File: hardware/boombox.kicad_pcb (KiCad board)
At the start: 4 copper layers, 125 x 107.9 mm, 92 parts, among them J1 Micro_SD_Card_Det1, J2 AudioJack4, J3 Battery, J4 USB_C_Receptacle_USB2.0_16P, U1 Pico, U10 MAX98365A, U2 TMAG5231, U3 TMAG5231, U4 TMAG5231, U5 TMAG5231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

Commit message: Almost done TM
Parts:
- removed C5, C6, C7, C8, C9: 1nF, Capacitor_SMD:C_0402_1005Metric_Pad0.74x0.62mm_HandSolder
- removed D6, D7, D8: D_Dual_CommonCathode_AAK_Split, Package_TO_SOT_SMD:SOT-23
- removed J3: Battery, boombox:EBAA02C
- removed LS1: Speaker, boombox:EBAA02C
- removed the REF** at (166.0, 36.4)
- removed the REF** at (144.0, 36.4)
- removed the REF** at (199.7, 71.7)
- removed RV1: 500k, boombox:Degson 3 Pin
- removed TP10, TP9: ~, boombox:TestPoint_Pad_2.0x2.0mm
- removed TP11: TestPoint_Small, boombox:TestPoint_Pad_2.0x2.0mm
- added J5: Screw_Terminal_01x07, boombox:1990054, B.Cu at (196.1, 76.7)
- J2: value AudioJack4 -> Screw_Terminal_01x07; footprint boombox:EBAA02C_Audio -> boombox:1990054
- TP1, TP2, TP3, TP4, TP5, TP6, TP7, TP8: value ~ -> TestPoint_Small; moved to B.Cu
- TP12: moved to B.Cu
- moved TP12 90.5 mm to (167.0, 44.3)
- moved C11 53.8 mm to (133.2, 71.7), turned to 180 degrees
- moved J2 52.5 mm to (183.3, 125.0)
- moved TP7 46.6 mm to (183.5, 104.8)
- moved D11 43.7 mm to (196.7, 87.2)
- moved TP6 39.9 mm to (183.7, 100.3), turned to 180 degrees
- moved C17 34.7 mm to (110.8, 91.2)
- moved TP8 31.3 mm to (143.0, 44.3), turned to 180 degrees
- moved TP4 26.6 mm to (159.0, 44.3), turned to 180 degrees
- moved TP2 26.2 mm to (151.0, 44.3), turned to 180 degrees
- moved C21 24.2 mm to (197.1, 107.4), turned to -90 degrees
- moved C20 21.7 mm to (171.6, 117.2)
- moved TP3 21.3 mm to (155.0, 44.3), turned to 180 degrees
- moved TP1 19.6 mm to (147.0, 44.3), turned to 180 degrees
- moved TP5 19.2 mm to (163.0, 44.3), turned to 180 degrees
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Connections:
- Q2 pad 3: /Power/BUTTONS0 -> /Power/BTN_LATCH
- Q5 pad 1: /Power/BUTTONS0 -> /Power/BTN_LATCH
- R3 pad 1: /Power/BUTTONS0 -> /Power/BTN_LATCH
- S1 pad 3: (no net) -> unconnected-(S1-NO_1-Pad3)
- S1 pad 6: (no net) -> unconnected-(S1-NO_2-Pad6)
- S2 pad 1: Net-(S2-NC_1) -> Net-(S1-NC_1)
- S2 pad 3: (no net) -> unconnected-(S2-NO_1-Pad3)
- S2 pad 6: (no net) -> unconnected-(S2-NO_2-Pad6)
- S3 pad 1: Net-(S3-NC_1) -> Net-(S1-NC_1)
- S3 pad 3: (no net) -> unconnected-(S3-NO_1-Pad3)
- S3 pad 6: (no net) -> unconnected-(S3-NO_2-Pad6)
- S4 pad 1: Net-(S4-NC_1) -> Net-(S1-NC_1)
- S4 pad 3: (no net) -> unconnected-(S4-NO_1-Pad3)
- S4 pad 6: (no net) -> unconnected-(S4-NO_2-Pad6)
- S5 pad 1: Net-(S5-NC_1) -> Net-(S1-NC_1)
- S5 pad 3: (no net) -> unconnected-(S5-NO_1-Pad3)
- S5 pad 6: (no net) -> unconnected-(S5-NO_2-Pad6)
- TP1 pad 1: Net-(S1-NC_1) -> Net-(S1-NC_2)
- TP2 pad 1: /Power/BUTTONS0 -> Net-(S2-NC_2)
- TP3 pad 1: Net-(S2-NC_1) -> Net-(S3-NC_2)
- TP4 pad 1: /Power/BUTTONS0 -> Net-(S4-NC_2)
- TP5 pad 1: Net-(S3-NC_1) -> Net-(S5-NC_2)
- TP6 pad 1: /Power/BUTTONS0 -> Net-(D12-A)
- TP7 pad 1: Net-(S4-NC_1) -> GND
- TP8 pad 1: /Power/BUTTONS0 -> Net-(S1-NC_1)
- U1 pad 15: Net-(S1-NC_2) -> Net-(J2-Pin_7)
- U1 pad 16: Net-(S2-NC_2) -> Net-(J2-Pin_6)
- U1 pad 17: Net-(S3-NC_2) -> Net-(J2-Pin_5)
- U1 pad 19: Net-(S4-NC_2) -> Net-(J2-Pin_4)
- U1 pad 20: Net-(S5-NC_2) -> Net-(J2-Pin_3)
- U8 pad A2: Net-(U8-OUTN) -> Net-(J5-Pin_4)
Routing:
- net /Power/BTN_LATCH: track 0.00 -> 114.3 mm, vias 0 -> 1
- net BTN_PWR: track 0.00 -> 109.3 mm, vias 0 -> 1
- net Net-(S1-NC_1): track 0.00 -> 101.9 mm, vias 0 -> 1
- net Net-(J2-Pin_6): track 0.00 -> 77.8 mm, vias 0 -> 1
- net Net-(J2-Pin_4): track 0.00 -> 77.8 mm, vias 0 -> 1
- net Net-(J2-Pin_3): track 0.00 -> 75.2 mm, vias 0 -> 1
- net Net-(J2-Pin_5): track 0.00 -> 73.3 mm, vias 0 -> 1
- net Net-(J2-Pin_7): track 0.00 -> 61.8 mm, vias 0 -> 1
- net /Power/MAG_SENSOR4: track 105.8 -> 55.8 mm
- net /Power/MAG_SENSOR3: track 119.6 -> 72.8 mm
- net Net-(S1-NC_2): track 0.00 -> 41.0 mm
- net Net-(S5-NC_2): track 0.00 -> 35.5 mm
- net /Power/CLOCK_ALARM: track 60.5 -> 95.6 mm
- net /Power/POWER IN: track 65.3 -> 41.1 mm, vias 3 -> 4
- net Net-(S2-NC_2): track 0.00 -> 23.0 mm
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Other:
- outline, holes or cut-outs redrawn
- board text added: "Batt+"
- board text added: "Batt-"

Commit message: Fixing warnings
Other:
- board text added: "1. SPK+ 2. SPK- 3. AUX+ 4. AUX- 5. POT+ 6. POT→ 7. POT-"
- board text added: "1. SW_PWR 2. WAKE 3. SW5 4. SW4 5. SW3 6. SW2 7. SW1"
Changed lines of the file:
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@@
 		(tags "capacitor handsolder")
 		(property "Reference" "C11"
-			(at -0.625 1.175 360)
+			(at -0.625 1.175 0)
 			(layer "F.SilkS")
 			(effects
@@
 		)
 		(property "Value" "0.1uF"
-			(at 0 1.16 360)
+			(at 0 1.16 0)
 			(layer "F.Fab")
 			(hide yes)
@@
 		)
 		(fp_text user "${REFERENCE}"
-			(at 0 0 360)
+			(at 0 0 0)
 			(layer "F.Fab")
 			(effects
@@
 		(tags "capacitor handsolder")
 		(property "Reference" "C10"
-			(at 0 -1.16 360)
+			(at 0 -1.16 0)
 			(layer "F.SilkS")
 			(effects
@@
 		)
 		(property "Value" "0.1uF"
-			(at 0 1.16 360)
+			(at 0 1.16 0)
 			(layer "F.Fab")
 			(hide yes)
@@
 		)
 		(fp_text user "${REFERENCE}"
-			(at 0 0 360)
+			(at 0 0 0)
 			(layer "F.Fab")
 			(effects
@@
 		(tags "SOD-123")
 		(property "Reference" "D11"
-			(at 0.425 2.325 360)
+			(at 0.425 2.325 0)
 			(layer "F.SilkS")
 			(hide yes)
@@
 		)
 		(property "Value" "D_Schottky"
-			(at 0 2.1 360)
+			(at 0 2.1 0)
 			(layer "F.Fab")
 			(hide yes)
@@
 		)
 		(fp_text user "${REFERENCE}"
-			(at 0 -1.85 360)
+			(at 0 -1.85 0)
 			(layer "F.SilkS")
 			(effects
@@
 			(at -0.020005 -2.282797 90)
 			(layer "F.SilkS")
+			(hide yes)
 			(effects
 				(font
@@
 		(tags "Connector")
 		(property "Reference" "J5"
-			(at 6.375 1.3 0)
+			(at 7.2 1.3 0)
 			(layer "B.SilkS")
 			(effects
@@
 			(layer "B.Fab")
 		)
-		(fp_text user "${REFERENCE}"
-			(at 6.375 1.3 0)
-			(layer "B.Fab")
-			(effects
-				(font
-					(size 1.27 1.27)
-					(thickness 0.254)
-				)
-				(justify mirror)
-			)
-		)
 		(pad "1" thru_hole circle
 			(at 0 0 180)
@@
 		(tags "SOT TO_SOT_SMD")
 		(property "Reference" "U3"
-			(at 0 -2.6 0)
+			(at 2.975 1.45 0)
 			(layer "B.SilkS")
 			(effects
@@
 		)
 	)
+	(gr_text "1. SW_PWR\n2. WAKE\n3. SW5\n4. SW4\n5. SW3\n6. SW2\n7. SW1\n"
+		(at 177.075 131.925 0)
+		(layer "B.SilkS")
+		(effects
+			(font
+				(size 1 1)
+				(thickness 0.1)
+			)
+			(justify left bottom mirror)
+		)
+	)
+	(gr_text "1. SPK+\n2. SPK-\n3. AUX+\n4. AUX-\n5. POT+\n6. POT→\n7. POT-\n"
+		(at 177.45 79.775 0)
+		(layer "B.SilkS")
+		(effects
+			(font
+				(size 1 1)
+				(thickness 0.1)
+			)
+			(justify left bottom mirror)
+		)
+	)
 	(gr_text "Boomy Jr. V1.0"
 		(at 104.1 126.05 0)
@@
 	)
 	(segment
-		(start 181.93375 83.445748)
-		(end 181.83375 83.545748)
-		(width 0.15)
+		(start 182.117422 84.317422)
+		(end 182.323892 84.317422)
+		(width 0.2)
 		(layer "F.Cu")
 		(net 8)
@@
 	)
 	(segment
+		(start 181.93375 82.60875)
+		(end 181.83375 82.70875)
+		(width 0.2)
+		(layer "F.Cu")
+		(net 8)
+	)
+	(segment
 		(start 176.98375 82.5175)
 		(end 176.98375 83.445748)
@@
 	)
 	(segment
-		(start 181.83375 83.9675)
-		(end 182.183753 84.317503)
+		(start 176.88375 83.545748)
+		(end 176.88375 83.9675)
 		(width 0.15)
 		(layer "F.Cu")
@@
 	)
 	(segment
-		(start 176.88375 83.545748)
-		(end 176.88375 83.9675)
-		(width 0.15)
+		(start 182.323892 84.317422)
+		(end 182.440935 84.317422)
+		(width 0.2)
 		(layer "F.Cu")
 		(net 8)
@@
 	)
 	(segment
-		(start 181.93375 82.5175)
-		(end 181.93375 83.445748)
-		(width 0.15)
-		(layer "F.Cu")
-		(net 8)
-	)
-	(segment
 		(start 175.14625 83.9625)
 		(end 175.15125 83.9675)
@@
 	)
 	(segment
-		(start 182.80875 83.9425)
-		(end 182.433747 84.317503)
-		(width 0.15)
+		(start 181.83375 82.70875)
+		(end 181.83375 84.03375)
+		(width 0.2)
 		(layer "F.Cu")
 		(net 8)
@@
 	)
 	(segment
+		(start 181.83375 84.03375)
+		(end 182.117422 84.317422)
+		(width 0.2)
+		(layer "F.Cu")
+		(net 8)
+	)
+	(segment
 		(start 137.9919 80.3075)
 		(end 137.9919 78.82)
@@
 	)
 	(segment
-		(start 182.183753 84.317503)
-		(end 182.33375 84.317503)
-		(width 0.15)
-		(layer "F.Cu")
-		(net 8)
-	)
-	(segment
 		(start 177.85875 83.9425)
 		(end 177.483747 84.317503)
@@
 	)
 	(segment
-		(start 181.83375 83.545748)
-		(end 181.83375 83.9675)
-		(width 0.15)
-		(layer "F.Cu")
-		(net 8)
-	)
-	(segment
 		(start 160.2625 80.5625)
 		(end 160.2 80.5)
@@
 	)
 	(segment
-		(start 182.433747 84.317503)
-		(end 182.33375 84.317503)
-		(width 0.15)
+		(start 182.440935 84.317422)
+		(end 182.812304 83.946053)
+		(width 0.2)
+		(layer "F.Cu")
+		(net 8)
+	)
+	(segment
+		(start 181.93375 82.5175)
+		(end 181.93375 82.60875)
+		(width 0.2)
 		(layer "F.Cu")
 		(net 8)
@@
 	)
 	(via
-		(at 182.33375 84.317503)
-		(size 0.4)
-		(drill 0.3)
-		(layers "F.Cu" "B.Cu")
-		(net 8)
-	)
-	(via
 		(at 181.225 86.925)
 		(size 0.6)
@@
 		(layers "F.Cu" "B.Cu")
 		(net 8)
+	)
+	(via
+		(at 182.323892 84.317422)
+		(size 0.4)
+		(drill 0.3)
+		(layers "F.Cu" "B.Cu")
+		(net 8)

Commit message: Fixed warnings
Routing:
- net Net-(U10-DAI1): vias 5 -> 4
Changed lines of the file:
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@@
 	)
 	(gr_text "1. SW_PWR\n2. WAKE\n3. SW5\n4. SW4\n5. SW3\n6. SW2\n7. SW1\n"
-		(at 177.075 131.925 0)
+		(at 179.825 131.525 0)
 		(layer "B.SilkS")
 		(effects
@@
 	)
 	(gr_text "1. SPK+\n2. SPK-\n3. AUX+\n4. AUX-\n5. POT+\n6. POT→\n7. POT-\n"
-		(at 177.45 79.775 0)
+		(at 179.425 79.75 0)
 		(layer "B.SilkS")
 		(effects
@@
 	)
 	(segment
+		(start 182.308357 84.45)
+		(end 182.812304 83.946053)
+		(width 0.2)
+		(layer "F.Cu")
+		(net 8)
+	)
+	(segment
 		(start 175.14625 81.20375)
 		(end 175.15 81.2)
@@
 	)
 	(segment
-		(start 182.117422 84.317422)
-		(end 182.323892 84.317422)
-		(width 0.2)
-		(layer "F.Cu")
-		(net 8)
-	)
-	(segment
 		(start 176.88375 83.9675)
 		(end 177.233753 84.317503)
@@
 	)
 	(segment
+		(start 181.975 84.45)
+		(end 182.308357 84.45)
+		(width 0.2)
+		(layer "F.Cu")
+		(net 8)
+	)
+	(segment
 		(start 177.78375 83.445748)
 		(end 177.85875 83.520748)
@@
 	)
 	(segment
+		(start 181.83375 84.03375)
+		(end 181.975 84.175)
+		(width 0.2)
+		(layer "F.Cu")
+		(net 8)
+	)
+	(segment
 		(start 176.98375 82.5175)
 		(end 176.98375 83.445748)
@@
 	)
 	(segment
-		(start 176.88375 83.545748)
-		(end 176.88375 83.9675)
-		(width 0.15)
+		(start 181.975 84.175)
+		(end 181.975 84.45)
+		(width 0.2)
 		(layer "F.Cu")
 		(net 8)
 	)
 	(segment
-		(start 182.323892 84.317422)
-		(end 182.440935 84.317422)
-		(width 0.2)
+		(start 176.88375 83.545748)
+		(end 176.88375 83.9675)
+		(width 0.15)
 		(layer "F.Cu")
 		(net 8)
@@
 	)
 	(segment
-		(start 181.83375 84.03375)
-		(end 182.117422 84.317422)
-		(width 0.2)
-		(layer "F.Cu")
-		(net 8)
-	)
-	(segment
 		(start 137.9919 80.3075)
 		(end 137.9919 78.82)
@@
 	)
 	(segment
-		(start 182.440935 84.317422)
-		(end 182.812304 83.946053)
-		(width 0.2)
-		(layer "F.Cu")
-		(net 8)
-	)
-	(segment
 		(start 181.93375 82.5175)
 		(end 181.93375 82.60875)
@@
 	)
 	(via
-		(at 137.8994 80.4)
-		(size 1)
-		(drill 0.6)
+		(at 181.975 84.45)
+		(size 0.4)
+		(drill 0.3)
 		(layers "F.Cu" "B.Cu")
 		(net 8)
 	)
 	(via
-		(at 182.323892 84.317422)
-		(size 0.4)
-		(drill 0.3)
+		(at 137.8994 80.4)
+		(size 1)
+		(drill 0.6)
 		(layers "F.Cu" "B.Cu")
 		(net 8)
@@
 	)
 	(via
-		(at 180.28375 86.2175)
-		(size 0.4)
-		(drill 0.3)
-		(layers "F.Cu" "B.Cu")
-		(net 38)
-	)
-	(via
 		(at 184.23375 82.1175)
 		(size 0.4)
@@
 	)
 	(segment
-		(start 180.28375 86.2175)
-		(end 179.88 86.62125)
+		(start 179.88 102.32)
+		(end 177.65 104.55)
 		(width 0.4)
 		(layer "B.Cu")
@@
 	)
 	(segment
-		(start 183.38375 82.9675)
-		(end 180.28375 82.9675)
-		(width 0.1)
+		(start 180.272687 82.972687)
+		(end 180.272687 85.588937)
+		(width 0.4)
 		(layer "B.Cu")
 		(net 38)
 	)
 	(segment
-		(start 179.88 86.62125)
-		(end 179.88 102.32)
+		(start 180.272687 85.588937)
+		(end 180.28375 85.6)
 		(width 0.4)
 		(layer "B.Cu")
@@
 	)
 	(segment
-		(start 184.23375 82.1175)
-		(end 183.38375 82.9675)
-		(width 0.1)
+		(start 180.28375 85.6)
+		(end 179.88 86.00375)
+		(width 0.4)
 		(layer "B.Cu")
 		(net 38)
 	)
 	(segment
-		(start 179.88 102.32)
-		(end 177.65 104.55)
+		(start 179.43375 82.13375)
+		(end 180.272687 82.972687)
 		(width 0.4)
 		(layer "B.Cu")
@@
 	)
 	(segment
-		(start 160.9975 104.5525)
-		(end 161 104.55)
+		(start 179.88 86.00375)
+		(end 179.88 102.32)
 		(width 0.4)
 		(layer "B.Cu")
@@
 	)
 	(segment
-		(start 180.28375 86.2175)
-		(end 180.28375 82.9675)
-		(width 0.1)
+		(start 160.9975 104.5525)
+		(end 161 104.55)
+		(width 0.4)
 		(layer "B.Cu")
 		(net 38)
@@
 	)
 	(segment
-		(start 180.28375 82.9675)
-		(end 179.43375 82.1175)
-		(width 0.1)
+		(start 180.272687 82.972687)
+		(end 183.378563 82.972687)
+		(width 0.4)
+		(layer "B.Cu")
+		(net 38)
+	)
+	(segment
+		(start 183.378563 82.972687)
+		(end 184.23375 82.1175)
+		(width 0.4)
+		(layer "B.Cu")
+		(net 38)
+	)
+	(segment
+		(start 179.43375 82.1175)
+		(end 179.43375 82.13375)
+		(width 0.4)
 		(layer "B.Cu")
 		(net 38)

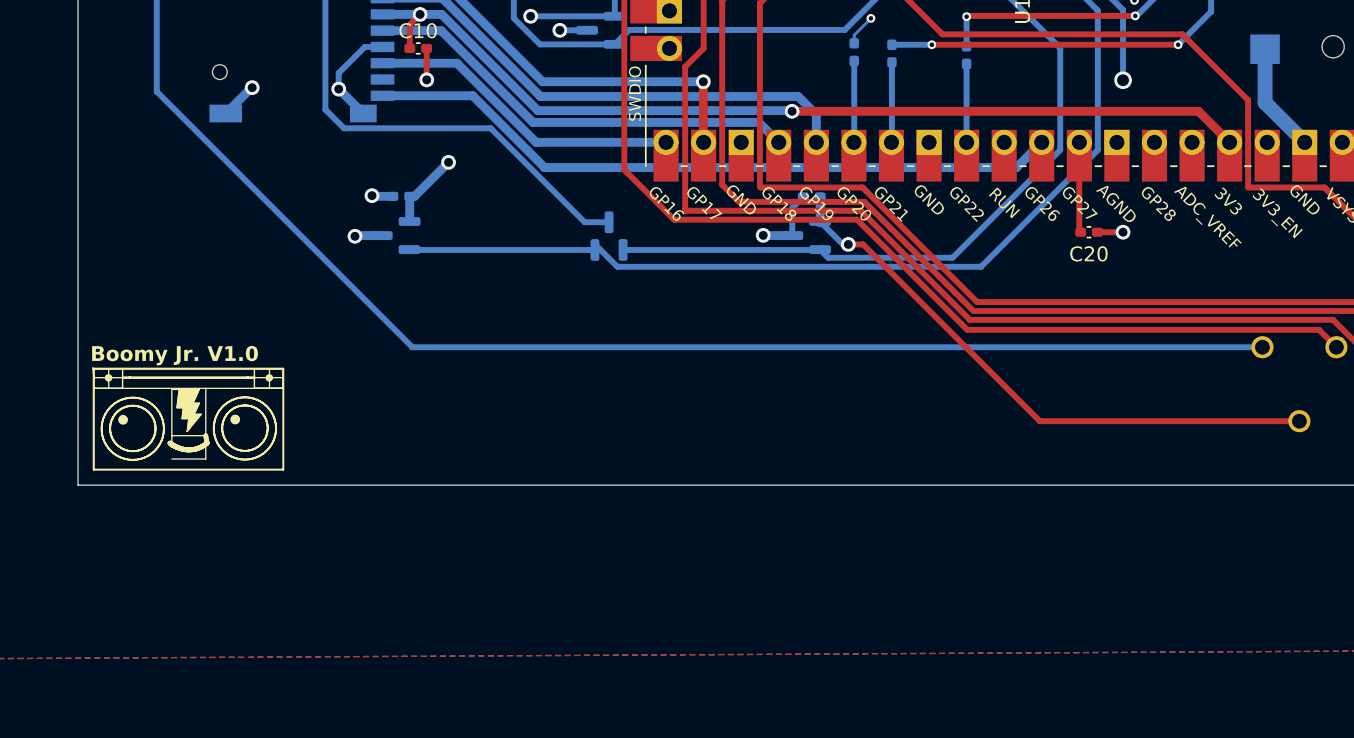
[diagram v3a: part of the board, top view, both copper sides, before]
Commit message: Added debouncing caps
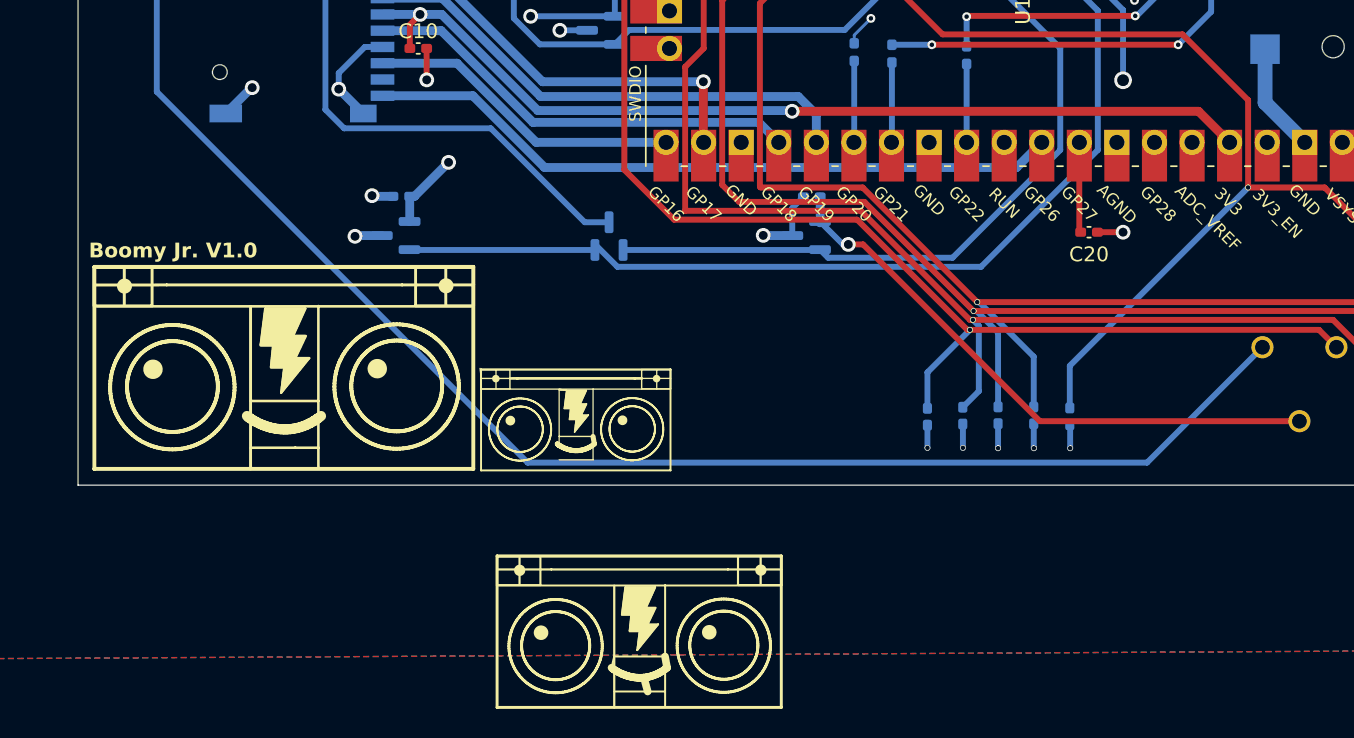
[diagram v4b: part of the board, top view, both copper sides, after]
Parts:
- added C5: .1u, Capacitor_SMD:C_0402_1005Metric_Pad0.74x0.62mm_HandSolder, B.Cu at (160.7, 129.7)
- added C6: .1u, Capacitor_SMD:C_0402_1005Metric_Pad0.74x0.62mm_HandSolder, B.Cu at (163.1, 129.6)
- added C7: .1u, Capacitor_SMD:C_0402_1005Metric_Pad0.74x0.62mm_HandSolder, B.Cu at (165.5, 129.6)
- added C8: .1u, Capacitor_SMD:C_0402_1005Metric_Pad0.74x0.62mm_HandSolder, B.Cu at (167.9, 129.6)
- added C9: .1u, Capacitor_SMD:C_0402_1005Metric_Pad0.74x0.62mm_HandSolder, B.Cu at (170.3, 129.7)
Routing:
- net Net-(J2-Pin_7): track 61.8 -> 81.7 mm, vias 1 -> 2
- net Net-(J2-Pin_6): track 77.8 -> 86.6 mm, vias 1 -> 2
- net GND: track 92.9 -> 100.9 mm, vias 31 -> 36
- net Net-(J2-Pin_5): track 73.3 -> 80.6 mm, vias 1 -> 2
- net Net-(J2-Pin_4): track 77.8 -> 84.3 mm, vias 1 -> 2
- net Net-(J2-Pin_3): track 75.2 -> 81.7 mm, vias 1 -> 2
- net /Power/BTN_LATCH: track 114.3 -> 120.7 mm
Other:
- board text added: "SW1"
- board text added: "SW2"
- board text added: "SW3"
- board text added: "SW4"
- board text added: "SW5"
- board text added: "SW_PWR"
- board text added: "WAKE"

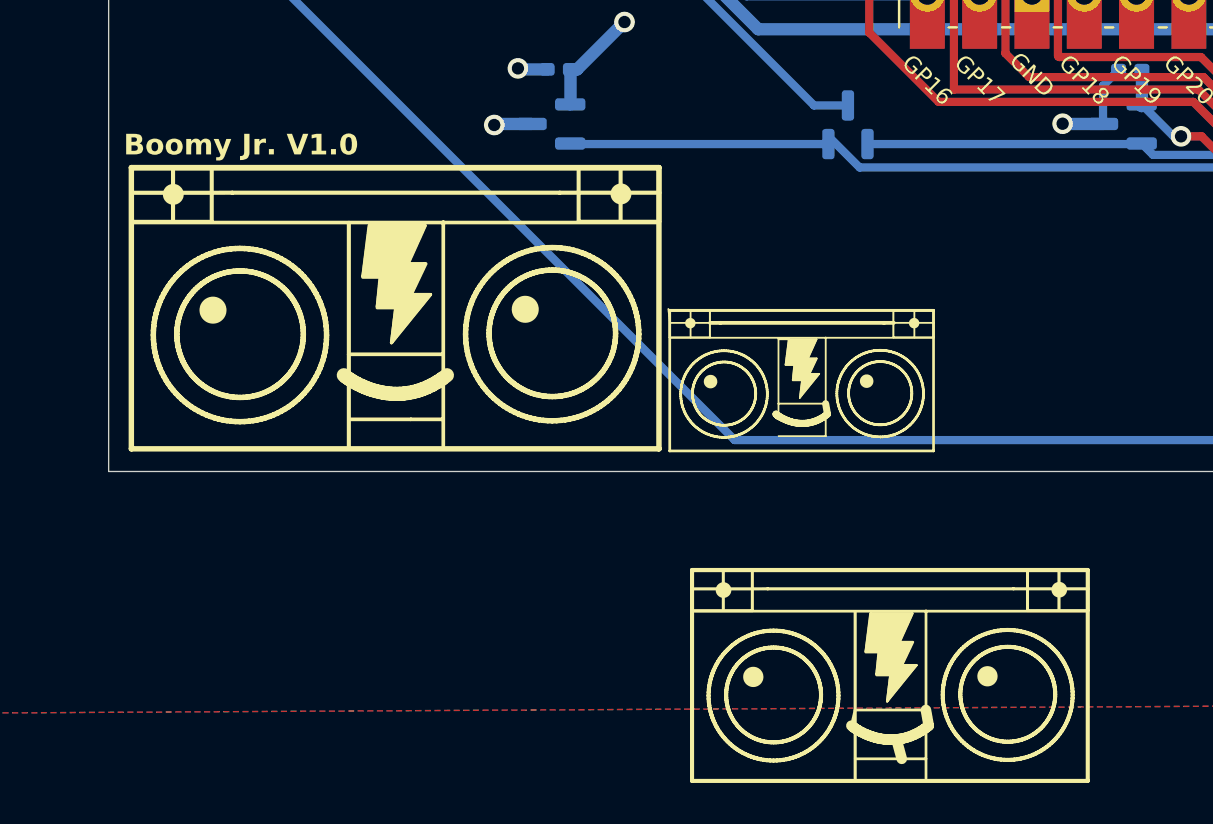
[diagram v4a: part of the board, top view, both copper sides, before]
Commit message: Updated logo
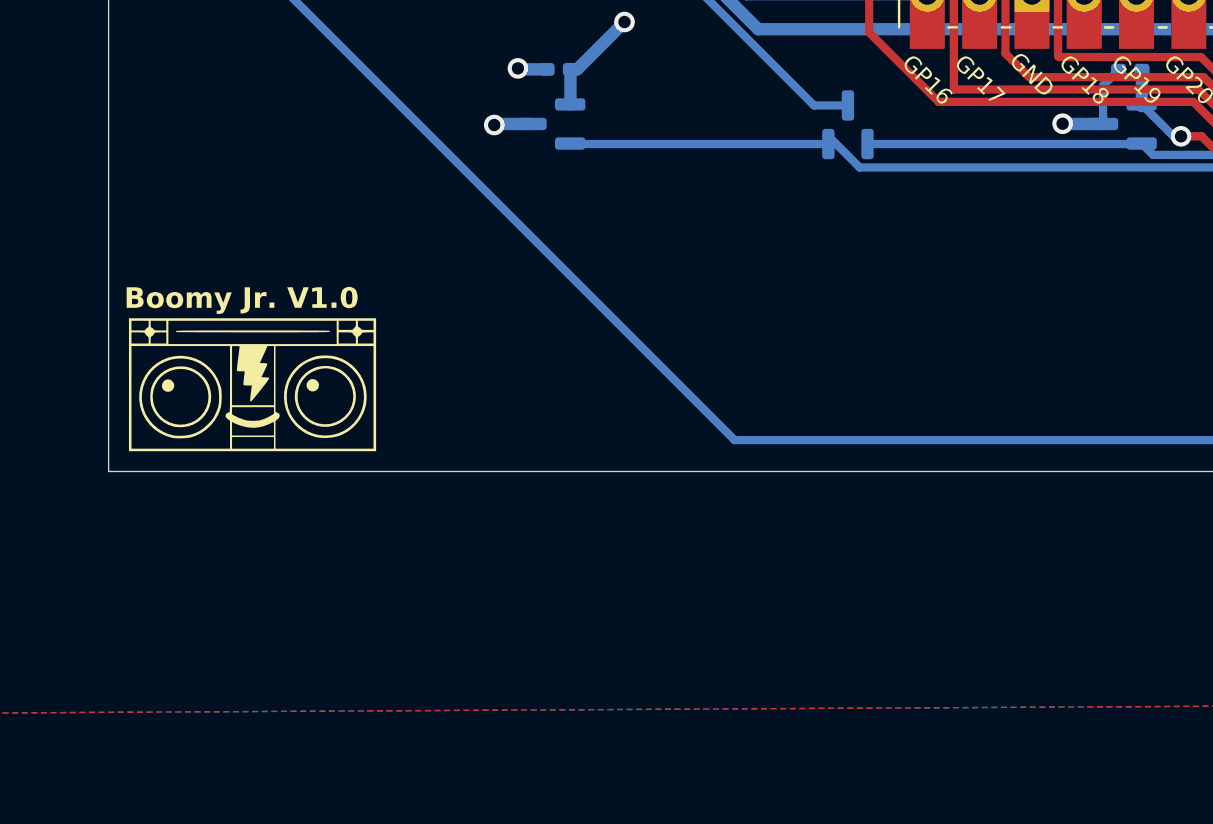
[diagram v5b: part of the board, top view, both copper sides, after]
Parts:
- added G***: LOGO, LOGO, F.Cu at (110.2, 130.1)
